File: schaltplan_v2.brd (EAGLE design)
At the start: 100 x 80 mm, 43 parts, among them T1 2N3565, T2 2N3565, T3 2N3565, T4 2N3565, T5 2N3565, T6 2N3565, T7 2N3565, T8 2N3565

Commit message: wiring fix
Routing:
- net N$19: track 296.6 -> 290.6 mm
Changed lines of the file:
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@@
 <wire x1="58.5" y1="71.12" x2="58.5" y2="66.04" width="0.4064" layer="16"/>
 <wire x1="58.5" y1="66.04" x2="86.36" y2="66.04" width="0.4064" layer="16"/>
-<wire x1="86.36" y1="55.88" x2="79" y2="55.88" width="0.4064" layer="16"/>
-<wire x1="79" y1="55.88" x2="76.2" y2="55.88" width="0.4064" layer="16"/>
-<wire x1="76.2" y1="55.88" x2="67" y2="55.88" width="0.4064" layer="16"/>
-<wire x1="67" y1="55.88" x2="64.77" y2="55.88" width="0.4064" layer="16"/>
-<wire x1="64.77" y1="55.88" x2="57" y2="55.88" width="0.4064" layer="16"/>
-<wire x1="57" y1="55.88" x2="54.61" y2="55.88" width="0.4064" layer="16"/>
-<wire x1="54.61" y1="55.88" x2="46" y2="55.88" width="0.4064" layer="16"/>
-<wire x1="46" y1="55.88" x2="43.18" y2="55.88" width="0.4064" layer="16"/>
-<wire x1="43.18" y1="55.88" x2="36" y2="55.88" width="0.4064" layer="16"/>
-<wire x1="36" y1="55.88" x2="33.02" y2="55.88" width="0.4064" layer="16"/>
-<wire x1="33.02" y1="55.88" x2="24" y2="55.88" width="0.4064" layer="16"/>
-<wire x1="24" y1="55.88" x2="21.59" y2="55.88" width="0.4064" layer="16"/>
-<wire x1="21.59" y1="55.88" x2="14" y2="55.88" width="0.4064" layer="16"/>
-<wire x1="14" y1="55.88" x2="13.43" y2="55.88" width="0.4064" layer="16"/>
+<wire x1="85.36" y1="53.88" x2="79" y2="53.88" width="0.4064" layer="16"/>
+<wire x1="79" y1="53.88" x2="76.2" y2="53.88" width="0.4064" layer="16"/>
+<wire x1="76.2" y1="53.88" x2="67" y2="53.88" width="0.4064" layer="16"/>
+<wire x1="67" y1="53.88" x2="64.77" y2="53.88" width="0.4064" layer="16"/>
+<wire x1="64.77" y1="53.88" x2="57" y2="53.88" width="0.4064" layer="16"/>
+<wire x1="57" y1="53.88" x2="54.61" y2="53.88" width="0.4064" layer="16"/>
+<wire x1="54.61" y1="53.88" x2="46" y2="53.88" width="0.4064" layer="16"/>
+<wire x1="46" y1="53.88" x2="43.18" y2="53.88" width="0.4064" layer="16"/>
+<wire x1="43.18" y1="53.88" x2="36" y2="53.88" width="0.4064" layer="16"/>
+<wire x1="36" y1="53.88" x2="33.02" y2="53.88" width="0.4064" layer="16"/>
+<wire x1="33.02" y1="53.88" x2="24" y2="53.88" width="0.4064" layer="16"/>
+<wire x1="24" y1="53.88" x2="21.59" y2="53.88" width="0.4064" layer="16"/>
+<wire x1="21.59" y1="53.88" x2="14" y2="53.88" width="0.4064" layer="16"/>
+<wire x1="14" y1="53.88" x2="13.43" y2="53.88" width="0.4064" layer="16"/>
 <contactref element="X4" pad="G1"/>
-<wire x1="13.43" y1="55.88" x2="7.62" y2="55.88" width="0.4064" layer="16"/>
-<wire x1="7.62" y1="55.88" x2="7.62" y2="72.39" width="0.4064" layer="16"/>
-<wire x1="7.62" y1="72.39" x2="19.2278" y2="72.39" width="0.4064" layer="16"/>
-<wire x1="14" y1="49.53" x2="14" y2="55.88" width="0.4064" layer="16"/>
+<wire x1="13.43" y1="53.88" x2="5.62" y2="53.88" width="0.4064" layer="16"/>
+<wire x1="5.62" y1="53.88" x2="5.62" y2="72.39" width="0.4064" layer="16"/>
+<wire x1="5.62" y1="72.39" x2="19.2278" y2="72.39" width="0.4064" layer="16"/>
+<wire x1="14" y1="49.53" x2="14" y2="53.88" width="0.4064" layer="16"/>
 <wire x1="24" y1="49.53" x2="24" y2="50" width="0.4064" layer="16"/>
-<wire x1="24" y1="50" x2="24" y2="55.88" width="0.4064" layer="16"/>
-<wire x1="36" y1="49.53" x2="36" y2="55.88" width="0.4064" layer="16"/>
-<wire x1="46" y1="49.53" x2="46" y2="55.88" width="0.4064" layer="16"/>
-<wire x1="57" y1="49.53" x2="57" y2="55.88" width="0.4064" layer="16"/>
+<wire x1="24" y1="50" x2="24" y2="53.88" width="0.4064" layer="16"/>
+<wire x1="36" y1="49.53" x2="36" y2="53.88" width="0.4064" layer="16"/>
+<wire x1="46" y1="49.53" x2="46" y2="53.88" width="0.4064" layer="16"/>
+<wire x1="57" y1="49.53" x2="57" y2="53.88" width="0.4064" layer="16"/>
 <wire x1="67" y1="49.53" x2="67" y2="50" width="0.4064" layer="16"/>
-<wire x1="67" y1="50" x2="67" y2="55.88" width="0.4064" layer="16"/>
-<wire x1="79" y1="49.53" x2="79" y2="55.88" width="0.4064" layer="16"/>
+<wire x1="67" y1="50" x2="67" y2="53.88" width="0.4064" layer="16"/>
+<wire x1="79" y1="49.53" x2="79" y2="53.88" width="0.4064" layer="16"/>
 <wire x1="11.43" y1="42.53" x2="14" y2="42.53" width="0.4064" layer="16"/>
 <wire x1="14" y1="42.53" x2="14" y2="49.53" width="0.4064" layer="16"/>
@@
 <wire x1="86.36" y1="66.04" x2="89" y2="66.04" width="0.4064" layer="16"/>
 <wire x1="89" y1="66.04" x2="89" y2="56" width="0.4064" layer="16"/>
-<wire x1="89" y1="56" x2="89" y2="49.53" width="0.4064" layer="16"/>
-<wire x1="86.36" y1="55.88" x2="89" y2="55.88" width="0.4064" layer="16"/>
-<wire x1="89" y1="55.88" x2="89" y2="56" width="0.4064" layer="16"/>
+<wire x1="89" y1="56" x2="89" y2="53.88" width="0.4064" layer="16"/>
+<wire x1="89" y1="53.88" x2="89" y2="49.53" width="0.4064" layer="16"/>
+<wire x1="85.36" y1="53.88" x2="89" y2="53.88" width="0.4064" layer="16"/>
+<wire x1="89" y1="53.88" x2="89" y2="56" width="0.4064" layer="16"/>
 <wire x1="58.5" y1="71.12" x2="58.5" y2="70.612" width="0" layer="19" extent="16-16"/>
 </signal>

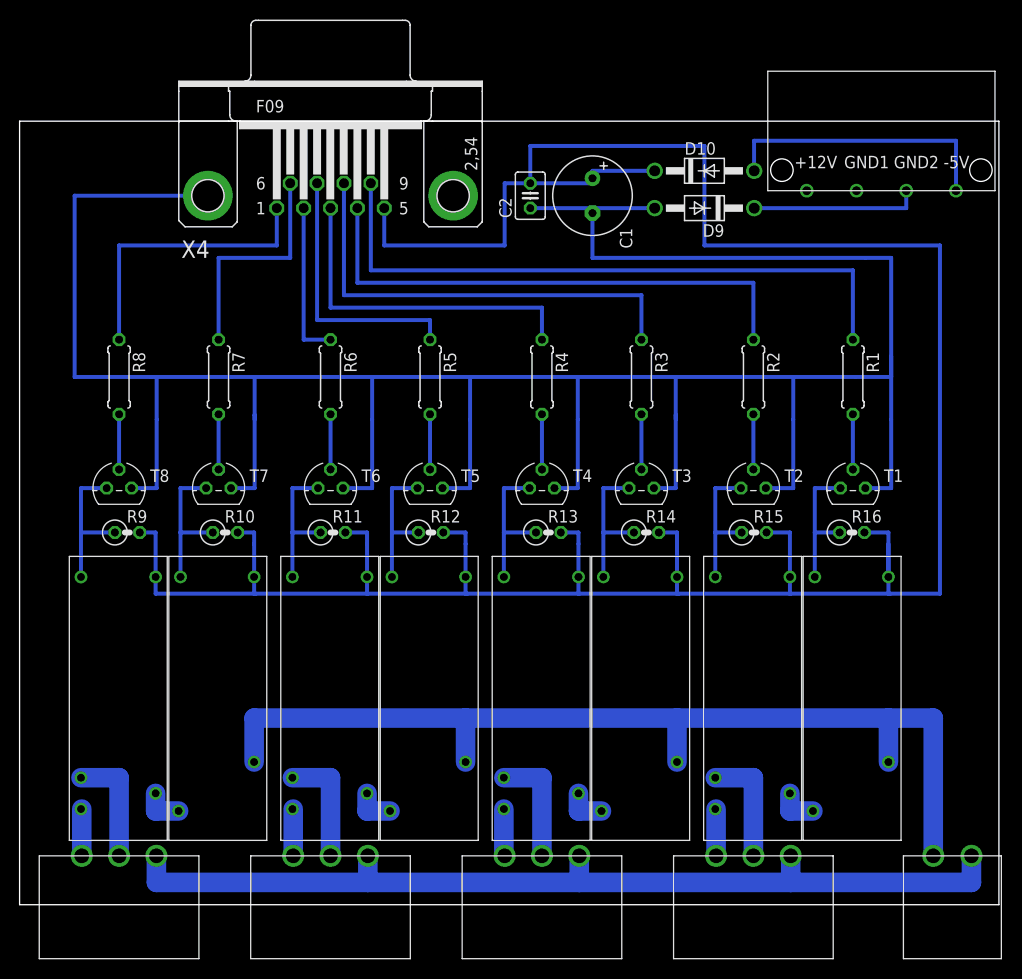
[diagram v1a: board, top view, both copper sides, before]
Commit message: fixed ground areas
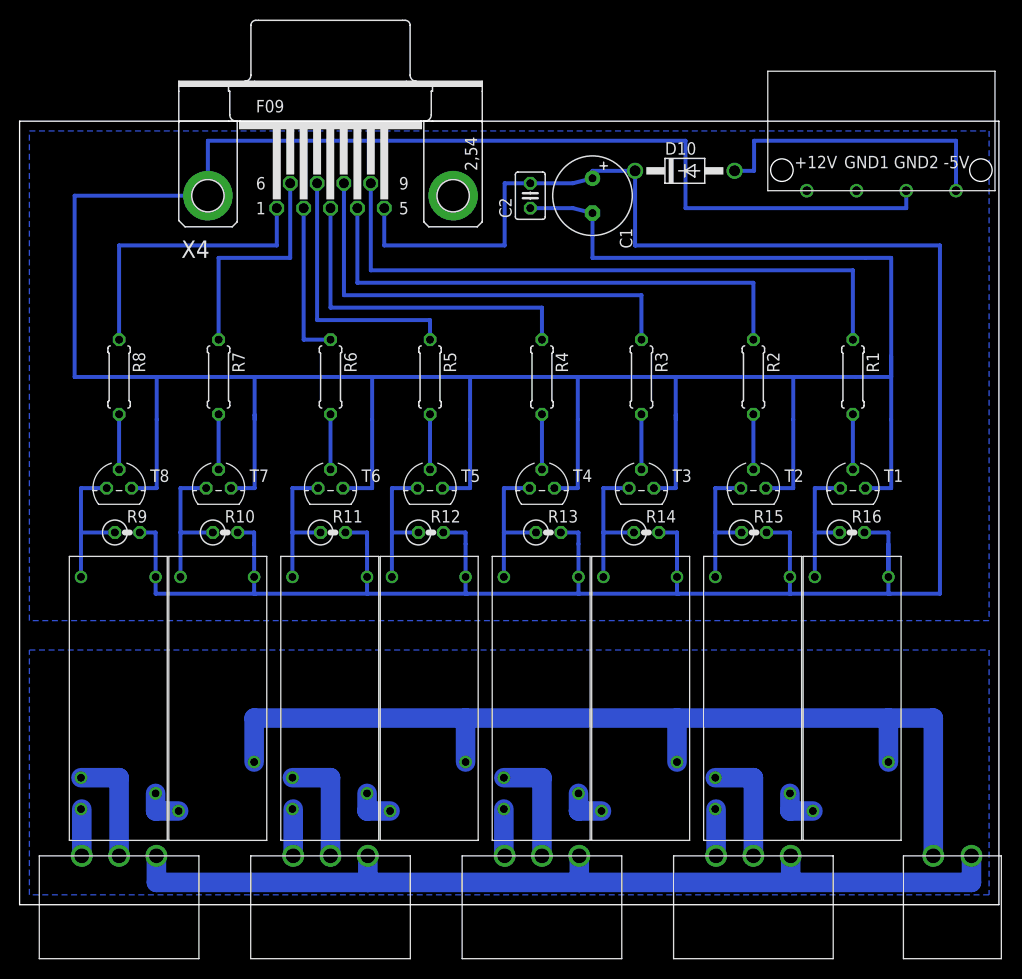
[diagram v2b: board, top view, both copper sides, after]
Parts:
- removed D9: 1N4004, diode:DO41-10
- moved D10 2.00 mm to (67.9, 74.9)
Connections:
- net N$1 renamed GND2
- removed net N$19: C1.-, C2.1, D9.A, T1.1, T2.1, T3.1, T4.1, T5.1, T6.1, T7.1, T8.1, X4.G1
- removed net N$9: D9.C, U$14.GND2
- new net GND: C1.-, C2.1, T1.1, T2.1, T3.1, T4.1, T5.1, T6.1, T7.1, T8.1, U$14.GND2, X4.G1
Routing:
- net GND: track 0.00 -> 369.4 mm
- net N$19: track 290.6 -> 0.00 mm
- net N$24: track 279.8 -> 260.3 mm
- net N$9: track 17.3 -> 0.00 mm
- net N$7: track 28.8 -> 30.8 mm
- added copper zone on layer 16, net GND
- added copper zone on layer 16, net GND2
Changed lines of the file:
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@@
 <element name="T7" library="transistor" package="TO92" value="2N3565" x="20.32" y="42.53"/>
 <element name="T8" library="transistor" package="TO92" value="2N3565" x="10.16" y="42.53"/>
-<element name="D9" library="diode" package="DO41-10" value="1N4004" x="69.93" y="71.12" rot="R180"/>
-<element name="D10" library="diode" package="DO41-10" value="1N4004" x="69.93" y="74.93"/>
+<element name="D10" library="diode" package="DO41-10" value="1N4004" x="67.93" y="74.93"/>
 <element name="C1" library="rcl" package="E3,5-8" value="" x="58.5" y="72.39" rot="R270"/>
 <element name="C2" library="rcl" package="C025-030X050" value="" x="52.15" y="72.39" rot="R90"/>
@@
 <contactref element="U$7" pad="P$2"/>
 <contactref element="U$8" pad="P$2"/>
-<wire x1="58.5" y1="74.93" x2="58.5" y2="74.168" width="0.4064" layer="16"/>
 <wire x1="57.07" y1="36.83" x2="57.07" y2="33.46" width="0.4064" layer="16"/>
 <wire x1="67.13" y1="36.83" x2="67.13" y2="33.46" width="0.4064" layer="16"/>
@@
 <wire x1="78.66" y1="33.46" x2="78.74" y2="33.46" width="0.4064" layer="16"/>
 <wire x1="49.53" y1="73.66" x2="52.15" y2="73.66" width="0.4064" layer="16"/>
-<wire x1="52.15" y1="73.66" x2="58.5" y2="73.66" width="0.4064" layer="16"/>
-<wire x1="58.5" y1="73.66" x2="58.5" y2="74.168" width="0.4064" layer="16"/>
-<wire x1="58.5" y1="74.93" x2="64.85" y2="74.93" width="0.4064" layer="16"/>
-<wire x1="52.15" y1="73.66" x2="52.15" y2="77.47" width="0.4064" layer="16"/>
-<wire x1="52.15" y1="77.47" x2="69.93" y2="77.47" width="0.4064" layer="16"/>
-<wire x1="69.93" y1="77.47" x2="69.93" y2="67.31" width="0.4064" layer="16"/>
-<wire x1="69.93" y1="67.31" x2="93.98" y2="67.31" width="0.4064" layer="16"/>
+<wire x1="52.15" y1="73.66" x2="56.5" y2="73.66" width="0.4064" layer="16"/>
+<wire x1="56.5" y1="73.66" x2="58.5" y2="74.168" width="0.4064" layer="16"/>
+<wire x1="62.93" y1="67.31" x2="93.98" y2="67.31" width="0.4064" layer="16"/>
 <wire x1="93.98" y1="67.31" x2="93.98" y2="31.75" width="0.4064" layer="16"/>
 <wire x1="93.98" y1="31.75" x2="88.9" y2="31.75" width="0.4064" layer="16"/>
@@
 <wire x1="65.27" y1="38" x2="67.13" y2="38" width="0.4064" layer="16"/>
 <wire x1="67.13" y1="38" x2="67.13" y2="36.83" width="0.4064" layer="16"/>
-</signal>
-<signal name="N$19">
+<wire x1="62.93" y1="67.31" x2="62.85" y2="67.31" width="0.4064" layer="16"/>
+<wire x1="62.85" y1="67.31" x2="62.85" y2="74.93" width="0.4064" layer="16"/>
+<wire x1="62.85" y1="74.93" x2="58.5" y2="74.93" width="0.4064" layer="16"/>
+<wire x1="58.5" y1="74.93" x2="58.5" y2="74.168" width="0.4064" layer="16"/>
+</signal>
+<signal name="GND">
 <contactref element="C1" pad="-"/>
 <contactref element="C2" pad="1"/>
-<wire x1="52.15" y1="71.12" x2="58.5" y2="71.12" width="0.4064" layer="16"/>
 <contactref element="T1" pad="1"/>
 <contactref element="T2" pad="1"/>
@@
 <contactref element="T8" pad="1"/>
 <contactref element="T7" pad="1"/>
-<contactref element="D9" pad="A"/>
-<wire x1="64.85" y1="71.12" x2="58.5" y2="71.12" width="0.4064" layer="16"/>
-<wire x1="58.5" y1="71.12" x2="58.5" y2="66.04" width="0.4064" layer="16"/>
-<wire x1="58.5" y1="66.04" x2="86.36" y2="66.04" width="0.4064" layer="16"/>
 <wire x1="85.36" y1="53.88" x2="79" y2="53.88" width="0.4064" layer="16"/>
 <wire x1="79" y1="53.88" x2="76.2" y2="53.88" width="0.4064" layer="16"/>
@@
 <wire x1="85.36" y1="53.88" x2="89" y2="53.88" width="0.4064" layer="16"/>
 <wire x1="89" y1="53.88" x2="89" y2="56" width="0.4064" layer="16"/>
-<wire x1="58.5" y1="71.12" x2="58.5" y2="70.612" width="0" layer="19" extent="16-16"/>
+<contactref element="U$14" pad="GND2"/>
+<wire x1="90.54" y1="71.12" x2="90.54" y2="72.9" width="0.4064" layer="16"/>
+<wire x1="90.54" y1="71.12" x2="68" y2="71.12" width="0.4064" layer="16"/>
+<wire x1="68" y1="71.12" x2="68" y2="78" width="0.4064" layer="16"/>
+<wire x1="68" y1="78" x2="19.2278" y2="78" width="0.4064" layer="16"/>
+<wire x1="19.2278" y1="78" x2="19.2278" y2="72.39" width="0.4064" layer="16"/>
+<wire x1="52.15" y1="71.12" x2="56.5" y2="71.12" width="0.4064" layer="16"/>
+<wire x1="56.5" y1="71.12" x2="58.5" y2="70.612" width="0.4064" layer="16"/>
+<polygon width="0.4064" layer="16">
+<vertex x="1" y="79"/>
+<vertex x="99" y="79"/>
+<vertex x="99" y="29"/>
+<vertex x="1" y="29"/>
+</polygon>
+<wire x1="86.36" y1="66.04" x2="58.5" y2="66.04" width="0.4064" layer="16"/>
+<wire x1="58.5" y1="66.04" x2="58.5" y2="70.612" width="0.4064" layer="16"/>
 </signal>
 <signal name="N$11">
@@
 <wire x1="35.8648" y1="64.77" x2="35.8648" y2="73.66" width="0.4064" layer="16"/>
 </signal>
-<signal name="N$1">
+<signal name="GND2">
 <contactref element="U$9" pad="P$1"/>
 <contactref element="U$10" pad="P$1"/>
@@
 <wire x1="13.97" y1="4.98" x2="13.97" y2="2.27" width="2" layer="16"/>
 <wire x1="13.97" y1="2.27" x2="35.56" y2="2.27" width="2" layer="16"/>
+<polygon width="0.4064" layer="16">
+<vertex x="1" y="1"/>
+<vertex x="1" y="26"/>
+<vertex x="99" y="26"/>
+<vertex x="99" y="1"/>
+</polygon>
 </signal>
 <signal name="N$7">
 <contactref element="U$14" pad="-5V"/>
 <contactref element="D10" pad="A"/>
-<wire x1="75.01" y1="74.93" x2="75" y2="74.93" width="0.4064" layer="16"/>
+<wire x1="73.01" y1="74.93" x2="75" y2="74.93" width="0.4064" layer="16"/>
 <wire x1="75" y1="74.93" x2="75" y2="78" width="0.4064" layer="16"/>
 <wire x1="75" y1="78" x2="95.62" y2="78" width="0.4064" layer="16"/>
 <wire x1="95.62" y1="78" x2="95.62" y2="72.9" width="0.4064" layer="16"/>
 </signal>
-<signal name="N$9">
-<contactref element="U$14" pad="GND2"/>
-<contactref element="D9" pad="C"/>
-<wire x1="75.01" y1="71.12" x2="90.54" y2="71.12" width="0.4064" layer="16"/>
-<wire x1="90.54" y1="71.12" x2="90.54" y2="72.9" width="0.4064" layer="16"/>
-</signal>
 <signal name="N$10">
 <contactref element="X4" pad="G2"/>
 </signal>
 </signals>
+<errors>
+</errors>
 </board>
 </drawing>

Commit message: minor layout fixes
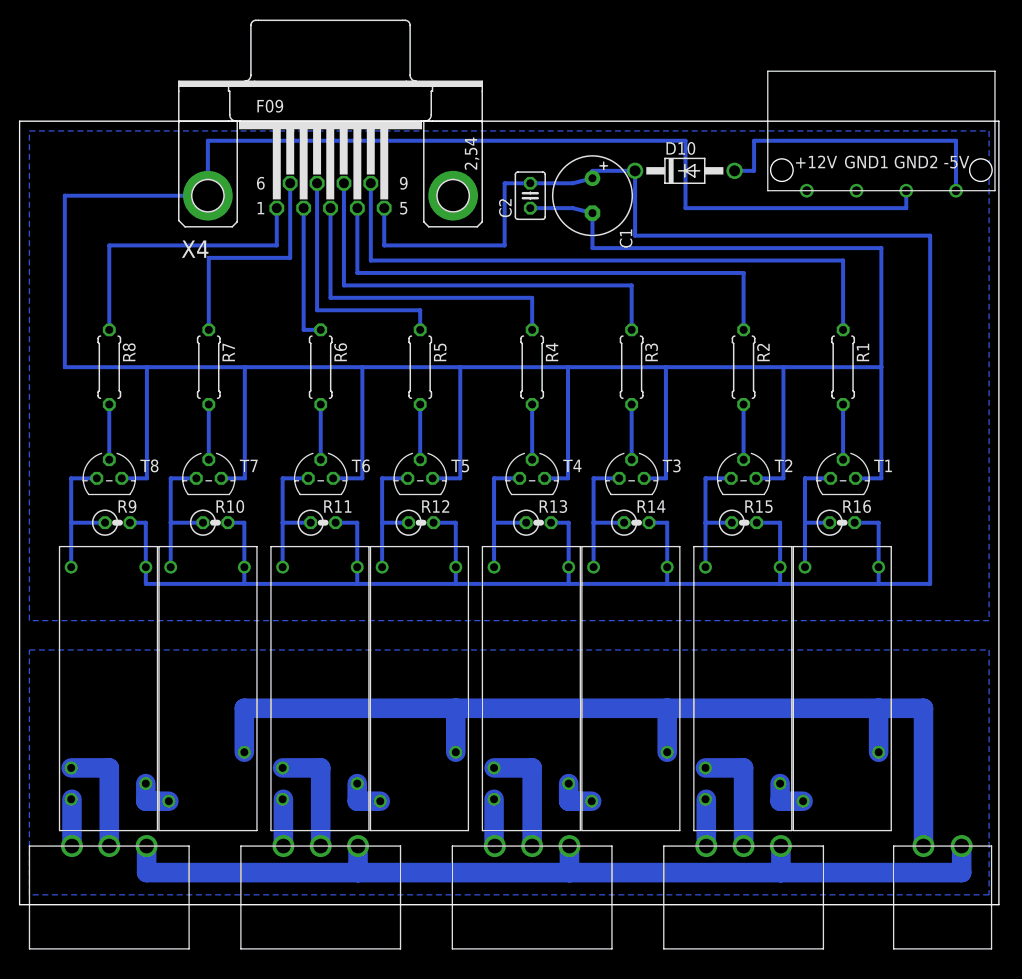
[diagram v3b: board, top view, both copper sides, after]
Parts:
- moved R1 1.41 mm to (84.1, 54.9)
- moved R10 1.41 mm to (20.0, 39.0)
- moved R11 1.41 mm to (31.0, 39.0)
- moved R12 1.41 mm to (41.0, 39.0)
- moved R13 1.41 mm to (53.0, 39.0)
- moved R14 1.41 mm to (63.0, 39.0)
- moved R15 1.41 mm to (74.0, 39.0)
- moved R16 1.41 mm to (84.0, 39.0)
- moved R2 1.41 mm to (73.9, 54.9)
- moved R3 1.41 mm to (62.5, 54.9)
- moved R4 1.41 mm to (52.3, 54.9)
- moved R5 1.41 mm to (40.9, 54.9)
- moved R6 1.41 mm to (30.8, 54.9)
- moved R7 1.41 mm to (19.3, 54.9)
- moved R8 1.41 mm to (9.16, 54.9)
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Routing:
- net GND: track 369.4 -> 364.4 mm
- net N$24: track 260.3 -> 255.4 mm
- net N$38: track 65.2 -> 63.2 mm
- net N$37: track 46.3 -> 44.3 mm
- net N$26: track 53.9 -> 51.9 mm
- net N$23: track 35.0 -> 33.0 mm
- net N$14: track 16.2 -> 14.2 mm
- net N$11: track 27.5 -> 25.5 mm
